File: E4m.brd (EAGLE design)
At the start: 50 x 100 mm, 78 parts, among them Q1 IRL540, Q2 IRL540, Q3 tip120

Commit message: routed
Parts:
- moved U$5 1.10 mm to (3.34, 8.46)
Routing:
- net GND: track 6.19 -> 355.4 mm, vias 0 -> 3
- net 5V: track 12.1 -> 215.0 mm, vias 0 -> 2
- net ENABLE: track 0.00 -> 84.0 mm, vias 0 -> 1
- net ANALOG: track 0.00 -> 71.9 mm
- net N$23: track 0.00 -> 71.4 mm, vias 0 -> 2
- net N$27: track 0.00 -> 70.8 mm, vias 0 -> 1
- net N$S4: track 0.00 -> 56.8 mm, vias 0 -> 1
- net E-STEP: track 0.00 -> 50.2 mm
- net X-DIR: track 0.00 -> 48.2 mm, vias 0 -> 1
- net S-A1: track 0.00 -> 43.2 mm, vias 0 -> 1
- net S-A0: track 0.00 -> 39.7 mm
- net 3V3: track 0.00 -> 37.3 mm
- net E-DIR: track 0.00 -> 35.0 mm, vias 0 -> 1
- net Z-STEP: track 0.00 -> 29.6 mm
- net X-STOP: track 0.00 -> 27.2 mm, vias 0 -> 1
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
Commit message: final?
mini4motion  esp4motion
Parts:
- removed JP7: (no value), pinhead:1X03
- added 12V-IN2: (no value), SparkFun:1X02
- moved X-MOT2 1.13 mm to (4.80, 82.0)
- moved R8 0.32 mm to (47.4, 91.3)
- moved U$6 0.32 mm to (22.4, 97.6)
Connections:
- removed net N$51: JP7.3, JP8.3
- net ENABLE1: now also JP8.3
- net N$52: now also 12V-IN2.2; no longer JP7.2
- net N$53: now also 12V-IN2.1; no longer JP7.1
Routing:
- net ENABLE1: track 0.00 -> 22.7 mm
- net N$51: track 15.7 -> 0.00 mm
- net N$42: track 34.4 -> 24.6 mm, vias 2 -> 1
- net 5V1: track 56.7 -> 63.7 mm, vias 3 -> 2
- net N$41: track 32.9 -> 26.1 mm, vias 4 -> 1
- net N$43: track 30.4 -> 24.6 mm, vias 0 -> 1
- net N$44: track 28.4 -> 25.3 mm, vias 0 -> 1
- net N$52: track 12.6 -> 9.80 mm
- net GND1: track 81.7 -> 78.9 mm, vias 2 -> 3
- net N$53: track 8.90 -> 6.49 mm
- net ANALOG: track 71.9 -> 70.5 mm
- net S-A0: track 39.7 -> 38.7 mm
- net Z-DIR1: track 43.6 -> 44.7 mm, vias 2 -> 1
- net S-A1: track 43.2 -> 42.2 mm
- net N$47: track 17.1 -> 16.2 mm
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- added copper zone on layer 1, net GND1
- added copper zone on layer 16, net GND1
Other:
- outline, holes or cut-outs redrawn

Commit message: last verified
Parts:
- removed E-MOT1, X-MOT1, X-MOT2, Y-MOT1, Z-MOT3: (no value), RepRapjr:1X04
- removed JP1, JP2, JP3: (no value), pinhead:1X03
- removed U$4: PCF8575TS, Ferduino:PCF8575TS
- added ANALOG: (no value), RepRapjr:1X04
- added IC1: MCP23017SS, adafruit:SSOP28
- added LED3: (no value), RepRapjr:CHIP-LED0805
- added R5: 22R, adafruit:R0805
- added R6: 10k, adafruit:R0805
- added X-S, Y-S, Z-S: (no value), pinhead:1X03
- E-MOT, X-MOT, Y-MOT, Z-MOT: device RepRapjr:1X04 -> adafruit:1X08-CLEANBIG
- Q3: value tip120 -> IRL540
- moved R14 62.3 mm to (18.9, 16.5)
- moved R10 46.2 mm to (19.0, 13.4), turned to 0 degrees
- moved AUX1 26.2 mm to (27.2, 38.9), turned to 0 degrees
- moved C6 18.8 mm to (19.5, 61.1), turned to 180 degrees
- moved Q1 15.8 mm to (17.4, 73.2)
- moved LED1 8.63 mm to (14.6, 65.7)
- moved R15 8.56 mm to (20.9, 65.7), turned to 90 degrees
- moved R12 8.54 mm to (16.5, 65.8), turned to 270 degrees
- moved R4 8.52 mm to (2.79, 72.8), turned to 270 degrees
- moved LM1117-5V 8.13 mm to (4.62, 62.5)
- moved D1 6.32 mm to (6.30, 73.2), turned to 90 degrees
- moved LED2 6.26 mm to (23.2, 65.8)
- moved JP4 6.22 mm to (9.20, 7.40), turned to 0 degrees
- moved 12V-IN 5.93 mm to (2.94, 81.2), turned to 0 degrees
- moved EXTRA 5.81 mm to (27.1, 60.8), turned to 0 degrees
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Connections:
- removed net N$61: U$3.2A, Y-MOT.2, Y-MOT1.2
- removed net N$62: U$3.1A, Y-MOT.3, Y-MOT1.3
- removed net N$63: U$3.1B, Y-MOT.4, Y-MOT1.4
- removed net N$68: U$9.2B, Z-MOT.1, Z-MOT3.1
- removed net N$69: U$9.2A, Z-MOT.2, Z-MOT3.2
- removed net N$70: U$9.1A, Z-MOT.3, Z-MOT3.3
- removed net N$71: U$9.1B, Z-MOT.4, Z-MOT3.4
- new net N$1: LED3.A, R5.1
- new net N$12: U$1.1B, X-MOT.4, X-MOT.8
- new net N$14: U$1.1A, X-MOT.3, X-MOT.7
- new net N$15: U$1.2A, X-MOT.2, X-MOT.6
- new net N$16: U$1.2B, X-MOT.1, X-MOT.5
- new net N$17: U$9.1B, Z-MOT.4, Z-MOT.8
- new net N$3: AUX2.2, IC1.7
- new net N$51: E-MOT.3, E-MOT.7, U$2.1A
- net 12V: now also FAN.1, R5.2; no longer FAN.2
- net 3V3: now also IC1.9; no longer U$4.24
- net 5V: now also X-S.3, Y-S.3, Z-S.3; no longer JP1.3, JP2.3, JP3.3
- net ANALOG: now also ANALOG.2, ANALOG.4; no longer X-MOT2.2, X-MOT2.4
- net AUX2: now also IC1.8; no longer U$4.20
- net E-DIR: now also IC1.24; no longer U$4.7
- net ENABLE: now also IC1.25; no longer U$4.8
- net GND: now also IC1.10, IC1.15, IC1.16, IC1.17, R6.2, X-S.2, Y-S.2, Z-S.2; no longer JP1.2, JP2.2, JP3.2, U$4.12, U$4.2, U$4.21, U$4.3
- net N$10: now also U$3.2A, Y-MOT.2, Y-MOT.6; no longer E-MOT.3, E-MOT1.3, U$2.1A
- net N$11: now also U$3.2B, Y-MOT.1, Y-MOT.5; no longer E-MOT.4, E-MOT1.4, U$2.1B
- net N$18: now also FAN.2, LED3.C; no longer FAN.1
- net N$19: now also IC1.3; no longer U$4.15
- net N$20: now also U$9.1A, Z-MOT.3, Z-MOT.7; no longer AUX2.2, U$4.19
- net N$21: now also IC1.6; no longer U$4.18
- net N$22: now also IC1.5; no longer U$4.17
- net N$26: now also IC1.4; no longer U$4.16
- net N$27: now also R6.1
- net N$46: now also U$9.2A, Z-MOT.2, Z-MOT.6; no longer U$1.2B, X-MOT.1, X-MOT1.1
- net N$48: now also U$9.2B, Z-MOT.1, Z-MOT.5; no longer U$1.2A, X-MOT.2, X-MOT1.2
- net N$50: now also E-MOT.4, E-MOT.8, U$2.1B; no longer U$1.1A, X-MOT.3, X-MOT1.3
- net N$55: now also E-MOT.2, E-MOT.6, U$2.2A; no longer U$1.1B, X-MOT.4, X-MOT1.4
- net N$60: now also E-MOT.1, E-MOT.5, U$2.2B; no longer U$3.2B, Y-MOT.1, Y-MOT1.1
- net N$8: now also U$3.1B, Y-MOT.4, Y-MOT.8; no longer E-MOT.1, E-MOT1.1, U$2.2B
- net N$9: now also U$3.1A, Y-MOT.3, Y-MOT.7; no longer E-MOT.2, E-MOT1.2, U$2.2A
- net S-A0: now also ANALOG.3, IC1.1; no longer U$4.13, X-MOT2.3
- net S-A1: now also ANALOG.1, IC1.2; no longer U$4.14, X-MOT2.1
- net SCL: now also IC1.12; no longer U$4.22
- net SDA: now also IC1.13; no longer U$4.23
- net X-DIR: now also IC1.21; no longer U$4.4
- net X-STOP: now also IC1.26, X-S.1; no longer JP1.1, U$4.9
- net Y-DIR: now also IC1.22; no longer U$4.5
- net Y-STOP: now also IC1.27, Y-S.1; no longer JP2.1, U$4.10
- net Z-DIR: now also IC1.23; no longer U$4.6
- net Z-STOP: now also IC1.28, Z-S.1; no longer JP3.1, U$4.11
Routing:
- net GND: track 355.4 -> 14.0 mm, vias 3 -> 2
- net 12V: track 146.4 -> 205.5 mm, vias 0 -> 1
- net 5V: track 215.0 -> 170.0 mm, vias 2 -> 0
- net S-A0: track 38.7 -> 5.82 mm
- net ANALOG: track 70.5 -> 39.3 mm
- net S-A1: track 42.2 -> 11.2 mm, vias 1 -> 0
- net N$8: track 4.58 -> 25.7 mm, vias 0 -> 1
- net N$23: track 71.4 -> 92.1 mm, vias 2 -> 1
- net N$9: track 4.58 -> 25.1 mm, vias 0 -> 2
- net N$11: track 4.58 -> 21.7 mm
- net N$51: track 0.00 -> 15.1 mm
- net N$17: track 0.00 -> 14.3 mm
- net N$16: track 0.00 -> 14.2 mm
- net N$12: track 0.00 -> 13.8 mm
- net N$S4: track 56.8 -> 70.5 mm
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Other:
- board size 50 x 100 mm -> 50.1 x 100 mm

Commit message: ready...
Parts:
- moved SJ18 0.79 mm to (38.9, 91.7)
- moved D1 0.68 mm to (6.81, 73.7)
- moved SJ17 0.56 mm to (36.6, 91.7)
- moved D2 0.56 mm to (42.1, 90.9)
- moved SJ15 0.28 mm to (34.2, 91.6)
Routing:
- net GND: track 14.0 -> 21.4 mm, vias 2 -> 3
- net 12V: track 205.5 -> 210.5 mm
- net 5V1: track 63.7 -> 66.6 mm
- net 12V1: track 40.2 -> 39.4 mm
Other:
- board text added: "Esp4Motion CC-BY-SA Misan Exilaus Darkberg"

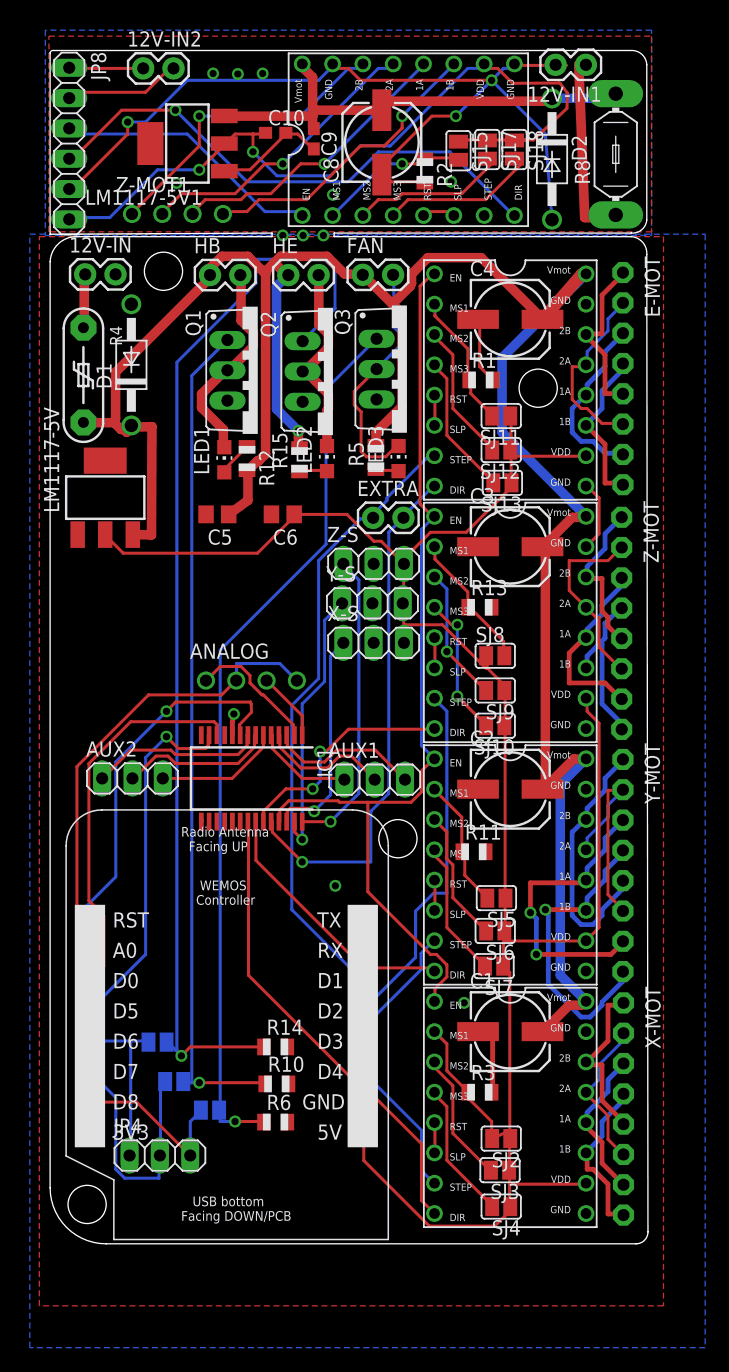
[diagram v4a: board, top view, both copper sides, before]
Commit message: ops
added servo output and panelized 100x100
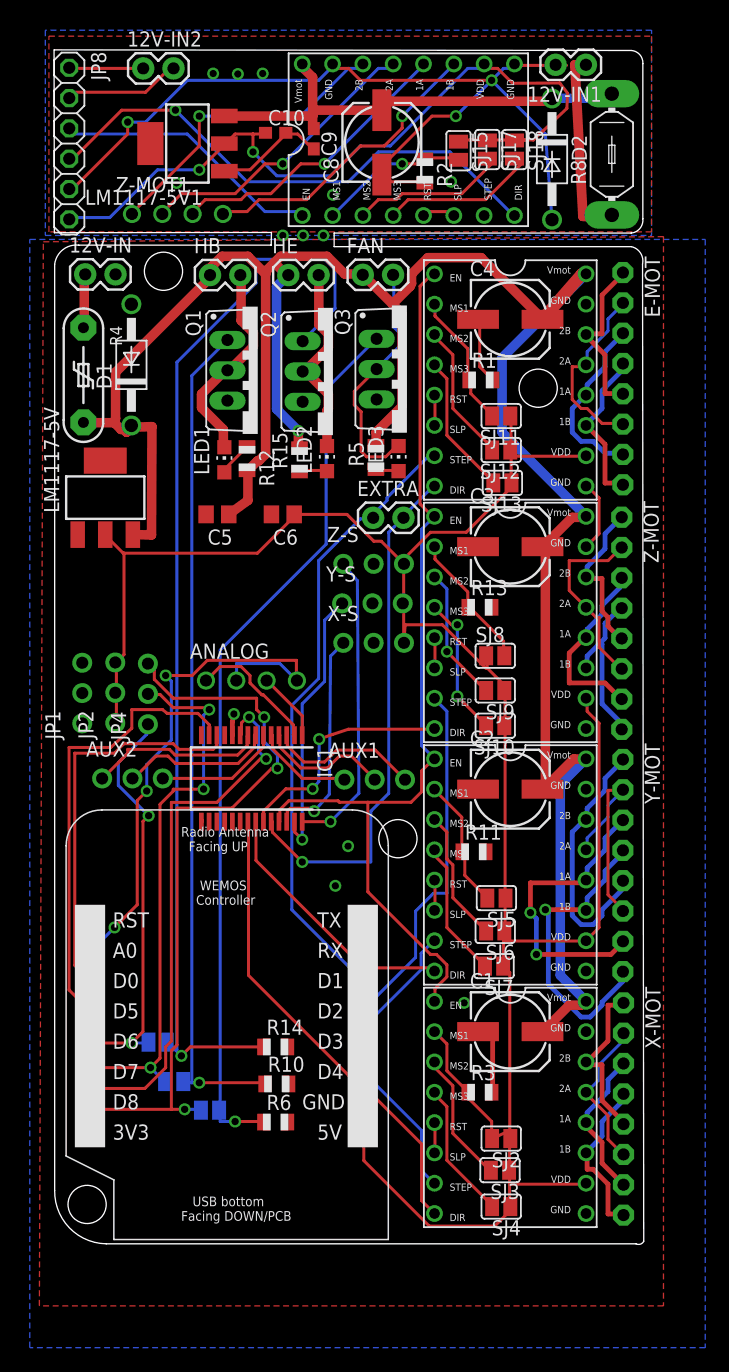
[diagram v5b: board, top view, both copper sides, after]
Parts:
- added JP1, JP2: (no value), adafruit:1X03-CLEANBIG
- AUX1, AUX2, JP4, X-S, Y-S, Z-S: device pinhead:1X03 -> adafruit:1X03-CLEANBIG
- JP8: device pinhead:1X06 -> adafruit:1X06
- moved JP4 38.7 mm to (8.20, 46.1), turned to 90 degrees
- moved R8 0.33 mm to (47.1, 91.3)
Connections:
- net 5V: now also JP2.1, JP2.2, JP2.3
- net GND: now also JP1.1, JP1.2, JP1.3
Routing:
- net FAN: track 14.4 -> 62.5 mm, vias 0 -> 3
- net HB0: track 21.3 -> 46.4 mm, vias 0 -> 3
- net HE0: track 14.6 -> 34.4 mm, vias 0 -> 2
- net 5V: track 170.0 -> 184.8 mm
- net SDA: track 30.6 -> 38.1 mm, vias 1 -> 0
- net ANALOG: track 39.3 -> 46.4 mm, vias 0 -> 3
- net 3V3: track 49.5 -> 50.2 mm, vias 1 -> 2
- net SCL: track 32.4 -> 33.0 mm
- net GND: vias 3 -> 4
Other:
- board size 50.1 x 100 mm -> 49.4 x 100.1 mm
- board text added: "12V-IN"
- board text added: "12V-IN1"
- board text added: "12V-IN2"
- board text added: "ANALOG"
- board text added: "AUX1"
- board text added: "AUX2"
- board text added: "C1"
- board text added: "C10"
- board text added: "C2"
- board text added: "C3"
- board text added: "C4"
- board text added: "C5"
- board text added: "C6"
- board text added: "C8"
- board text added: "C9"
- board text added: "D1"
- board text added: "D2"
- board text added: "E-MOT"
- board text added: "EXTRA"
- board text added: "FAN"
- board text added: "HB"
- board text added: "HE"
- board text added: "IC1"
- board text added: "JP1"
- board text added: "JP2"
- board text added: "JP4"
- board text added: "JP8"
- board text added: "LED1"
- board text added: "LED2"
- board text added: "LED3"
- board text added: "LM1117-5V"
- board text added: "LM1117-5V1"
- board text added: "Q1"
- board text added: "Q2"
- board text added: "Q3"
- board text added: "R1"
- board text added: "R10"
- board text added: "R11"
- board text added: "R12"
- board text added: "R13"
- board text added: "R14"
- board text added: "R15"
- board text added: "R2"
- board text added: "R3"
- board text added: "R4"
- board text added: "R5"
- board text added: "R6"
- board text added: "R8"
- board text added: "SJ1"
- board text added: "SJ10"
- board text added: "SJ11"
- board text added: "SJ12"
- board text added: "SJ13"
- board text added: "SJ14"
- board text added: "SJ15"
- board text added: "SJ16"
- board text added: "SJ17"
- board text added: "SJ18"
- board text added: "SJ2"
- board text added: "SJ3"
- board text added: "SJ4"
- board text added: "SJ5"
- board text added: "SJ6"
- board text added: "SJ7"
- board text added: "SJ8"
- board text added: "SJ9"
- board text added: "X-MOT"
- board text added: "X-S"
- board text added: "Y-MOT"
- board text added: "Y-S"
- board text added: "Z-MOT"
- board text added: "Z-MOT1"
- board text added: "Z-S"

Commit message: correct issue
need re-route   add all smd as 0805
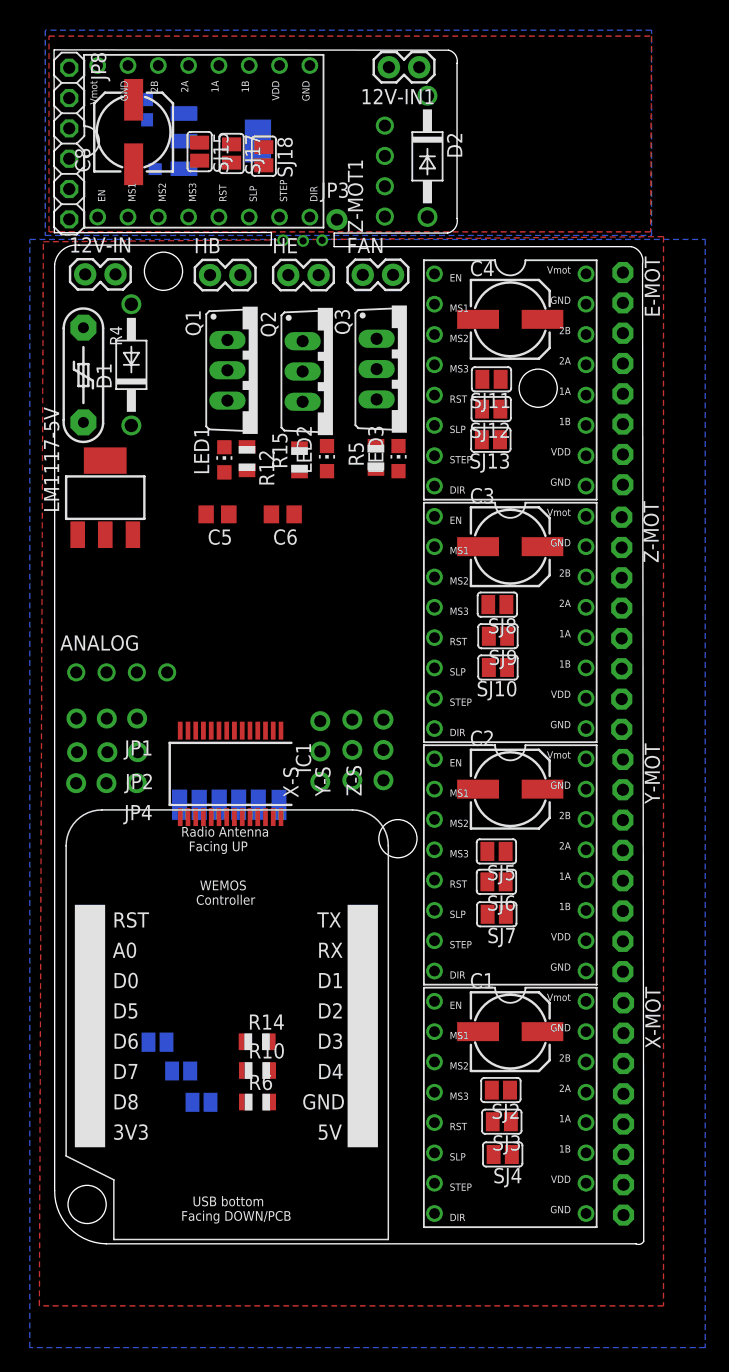
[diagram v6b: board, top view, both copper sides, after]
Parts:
- removed 12V-IN2, EXTRA: (no value), SparkFun:1X02
- removed AUX1, AUX2: (no value), adafruit:1X03-CLEANBIG
- removed R1, R11, R13, R2, R3: 100k, adafruit:R0805
- removed R8: 11, RepRapjr:LITTLEFUSE
- added JP3: (no value), adafruit:1X01-CLEANBIG
- added PAD1, PAD2, PAD3, PAD4, PAD5, PAD6: WIREPADSMD1,27-254, wirepad:SMD1,27-2,54
- moved SJ15 21.7 mm to (12.5, 91.5)
- moved SJ17 21.4 mm to (15.2, 91.4)
- moved SJ18 21.0 mm to (17.9, 91.1)
- moved C8 20.8 mm to (7.00, 93.2)
- moved Z-MOT1 18.8 mm to (28.1, 88.6), turned to 90 degrees
- moved U$6 17.1 mm to (5.25, 97.5)
- moved Z-S 15.6 mm to (27.9, 41.4), turned to 90 degrees
- moved C9 14.2 mm to (8.13, 95.0), flipped to the bottom
- moved 12V-IN1 14.0 mm to (30.9, 98.6)
- moved Y-S 12.4 mm to (25.3, 41.4), turned to 90 degrees
- moved C10 11.4 mm to (7.95, 90.1), flipped to the bottom, turned to 180 degrees
- moved ANALOG 10.9 mm to (4.73, 47.9)
- moved D2 10.4 mm to (31.6, 91.1)
- moved X-S 10.1 mm to (22.6, 41.3), turned to 90 degrees
- moved JP4 8.25 mm to (4.72, 38.6), turned to 180 degrees
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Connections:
- removed net N$47: 12V-IN1.1, R8.1
- removed net N$52: 12V-IN2.2, JP8.2
- removed net N$53: 12V-IN2.1, JP8.1
- new net 3V31: JP3.1, SJ15.1, SJ17.1, SJ18.1, U$6.VDD
- net 12V1: now also 12V-IN1.1; no longer R8.2
- net 3V3: now also SJ10.1, SJ11.1, SJ12.1, SJ13.1, SJ2.1, SJ3.1, SJ4.1, SJ5.1, SJ6.1, SJ7.1, SJ8.1, SJ9.1, U$1.VDD, U$2.VDD, U$3.VDD, U$9.VDD
- net 5V: no longer SJ10.1, SJ11.1, SJ12.1, SJ13.1, SJ2.1, SJ3.1, SJ4.1, SJ5.1, SJ6.1, SJ7.1, SJ8.1, SJ9.1, U$1.VDD, U$2.VDD, U$3.VDD, U$9.VDD
- net 5V1: no longer SJ15.1, SJ17.1, SJ18.1, U$6.VDD
- net ANALOG: now also ANALOG.1; no longer ANALOG.2
- net AUX2: now also PAD1.1; no longer AUX2.1
- net E-DIR: no longer EXTRA.2
- net E-STEP: now also U$5.D0; no longer EXTRA.1, U$5.D1
- net GND: no longer R1.2, R11.2, R13.2, R3.2
- net GND1: no longer R2.2
- net HB0: now also JP4.1; no longer JP4.2
- net HE0: now also JP4.2; no longer JP4.1
- net N$19: now also PAD6.1; no longer AUX1.3
- net N$21: now also PAD2.1; no longer AUX2.3
- net N$22: now also PAD4.1; no longer AUX1.1
- net N$26: now also PAD5.1; no longer AUX1.2
- net N$3: now also PAD3.1; no longer AUX2.2
- net N$35: no longer R3.1
- net N$40: no longer R2.1
- net N$59: no longer R11.1
- net N$67: no longer R13.1
- net N$7: no longer R1.1
- net S-A1: now also ANALOG.2; no longer ANALOG.1
- net SCL: now also U$5.D1; no longer U$5.D0
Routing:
- net 12V: track 210.5 -> 0.00 mm, vias 1 -> 0
- net 5V: track 184.8 -> 0.00 mm
- net N$23: track 92.1 -> 0.00 mm, vias 1 -> 0
- net ENABLE: track 79.8 -> 0.00 mm
- net GND1: track 78.9 -> 0.00 mm, vias 9 -> 0
- net N$27: track 74.8 -> 0.00 mm, vias 1 -> 0
- net N$S4: track 70.5 -> 0.00 mm, vias 1 -> 0
- net 5V1: track 66.6 -> 0.00 mm, vias 2 -> 0
- net FAN: track 62.5 -> 0.00 mm, vias 3 -> 0
- net E-STEP: track 52.2 -> 0.00 mm
- net 3V3: track 50.2 -> 0.18 mm, vias 2 -> 0
- net HB0: track 46.4 -> 0.00 mm, vias 3 -> 0
- net ANALOG: track 46.4 -> 0.00 mm, vias 3 -> 0
- net Z-DIR1: track 44.7 -> 0.00 mm, vias 1 -> 0
- net E-DIR: track 44.2 -> 0.00 mm, vias 1 -> 0
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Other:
- outline, holes or cut-outs redrawn
